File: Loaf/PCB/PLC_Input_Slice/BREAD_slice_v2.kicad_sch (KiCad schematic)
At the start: 26 parts, among them J1 10018783-10200TLF, J3 DB25_Socket, U1 MCP4922-EP, U2 MCP4922-EP, U3 MCP4922-EP, U4 MCP4922-EP, U5 MCP3208, U6 MCP2561-E-P, U7 MCP2515-xSO, Y1 16MHZ Crystal

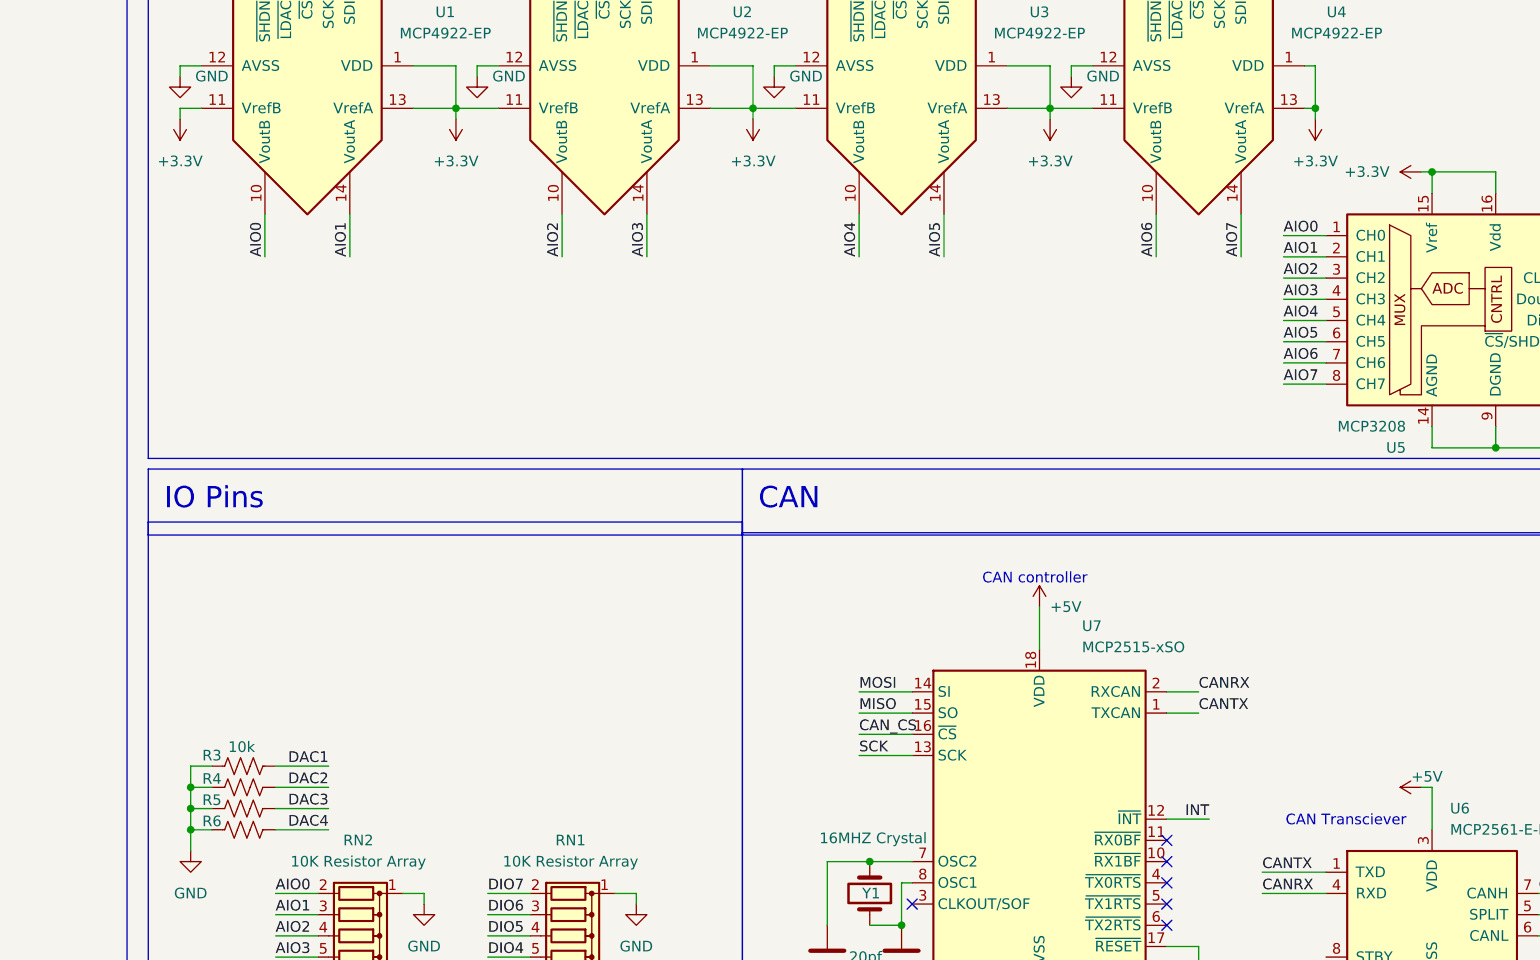
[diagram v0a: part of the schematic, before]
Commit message: Added optional VRM and switched to 5V ADC and DAC
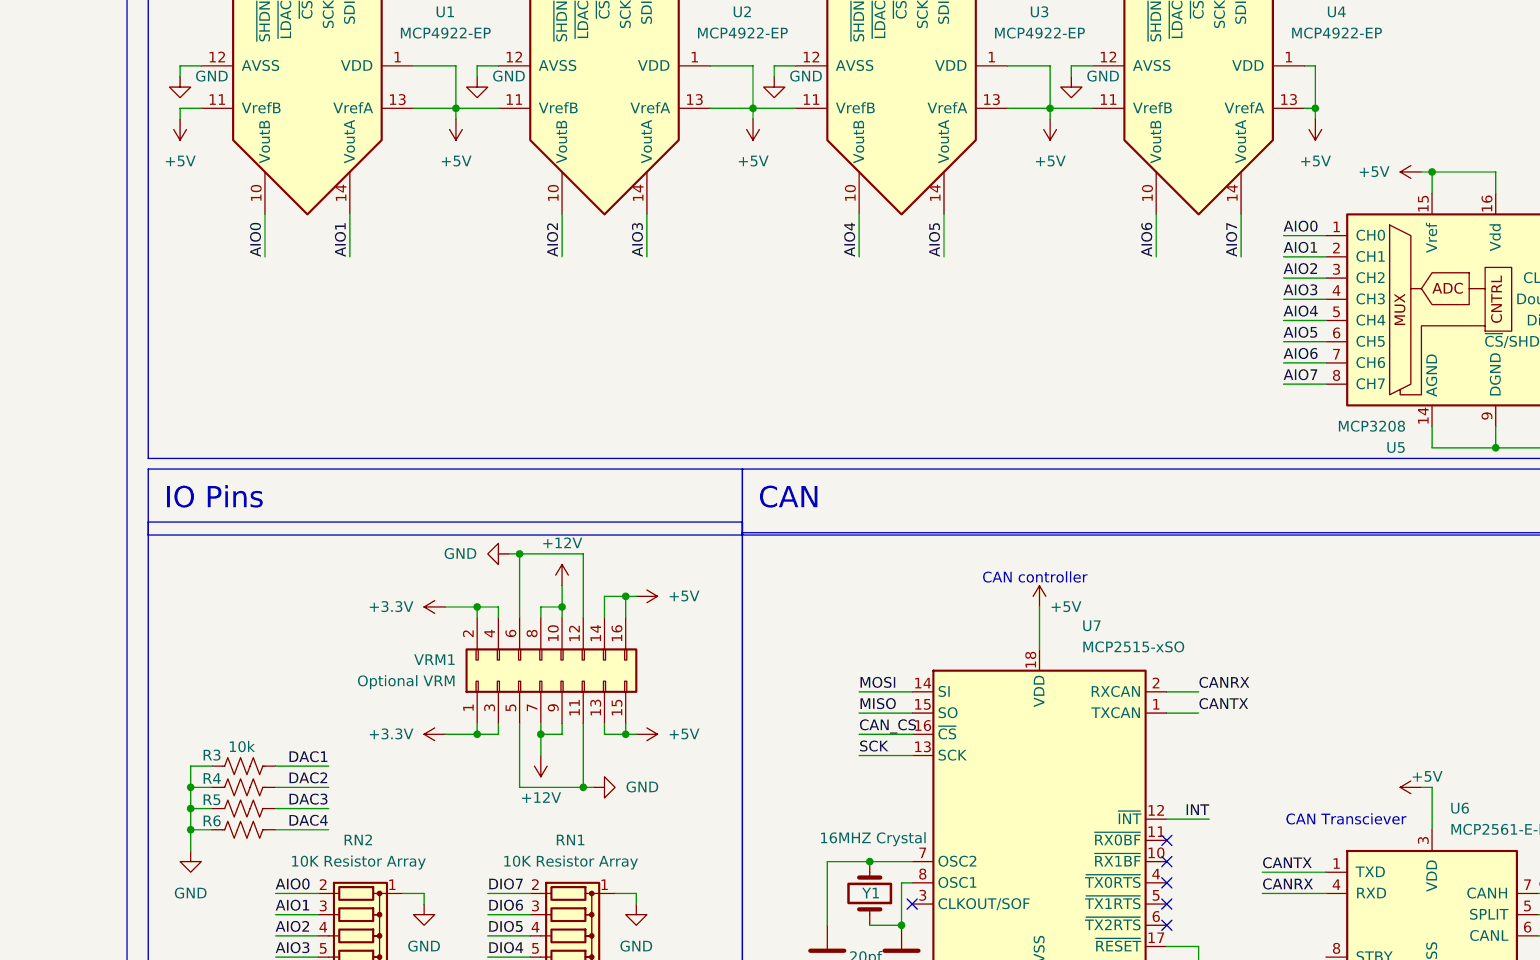
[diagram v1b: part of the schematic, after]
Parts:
- added VRM1: Optional VRM, PinSocket_2x08_P2.54mm_Vertical, symbol Connector_Generic:Conn_02x08_Odd_Even
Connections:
- net +12V: now also VRM1.10 (Pin_10), VRM1.7 (Pin_7), VRM1.8 (Pin_8), VRM1.9 (Pin_9)
- net +3.3V: now also VRM1.1 (Pin_1), VRM1.2 (Pin_2), VRM1.3 (Pin_3), VRM1.4 (Pin_4); no longer U1.1 (VDD), U1.11 (VrefB), U1.13 (VrefA), U2.1 (VDD), U2.11 (VrefB), U2.13 (VrefA), U3.1 (VDD), U3.11 (VrefB), U3.13 (VrefA), U4.1 (VDD), U4.11 (VrefB), U4.13 (VrefA), U5.15 (Vref), U5.16 (Vdd)
- net +5V: now also U1.1 (VDD), U1.11 (VrefB), U1.13 (VrefA), U2.1 (VDD), U2.11 (VrefB), U2.13 (VrefA), U3.1 (VDD), U3.11 (VrefB), U3.13 (VrefA), U4.1 (VDD), U4.11 (VrefB), U4.13 (VrefA), U5.15 (Vref), U5.16 (Vdd), VRM1.13 (Pin_13), VRM1.14 (Pin_14), VRM1.15 (Pin_15), VRM1.16 (Pin_16)
- net GND: now also VRM1.11 (Pin_11), VRM1.12 (Pin_12), VRM1.5 (Pin_5), VRM1.6 (Pin_6)

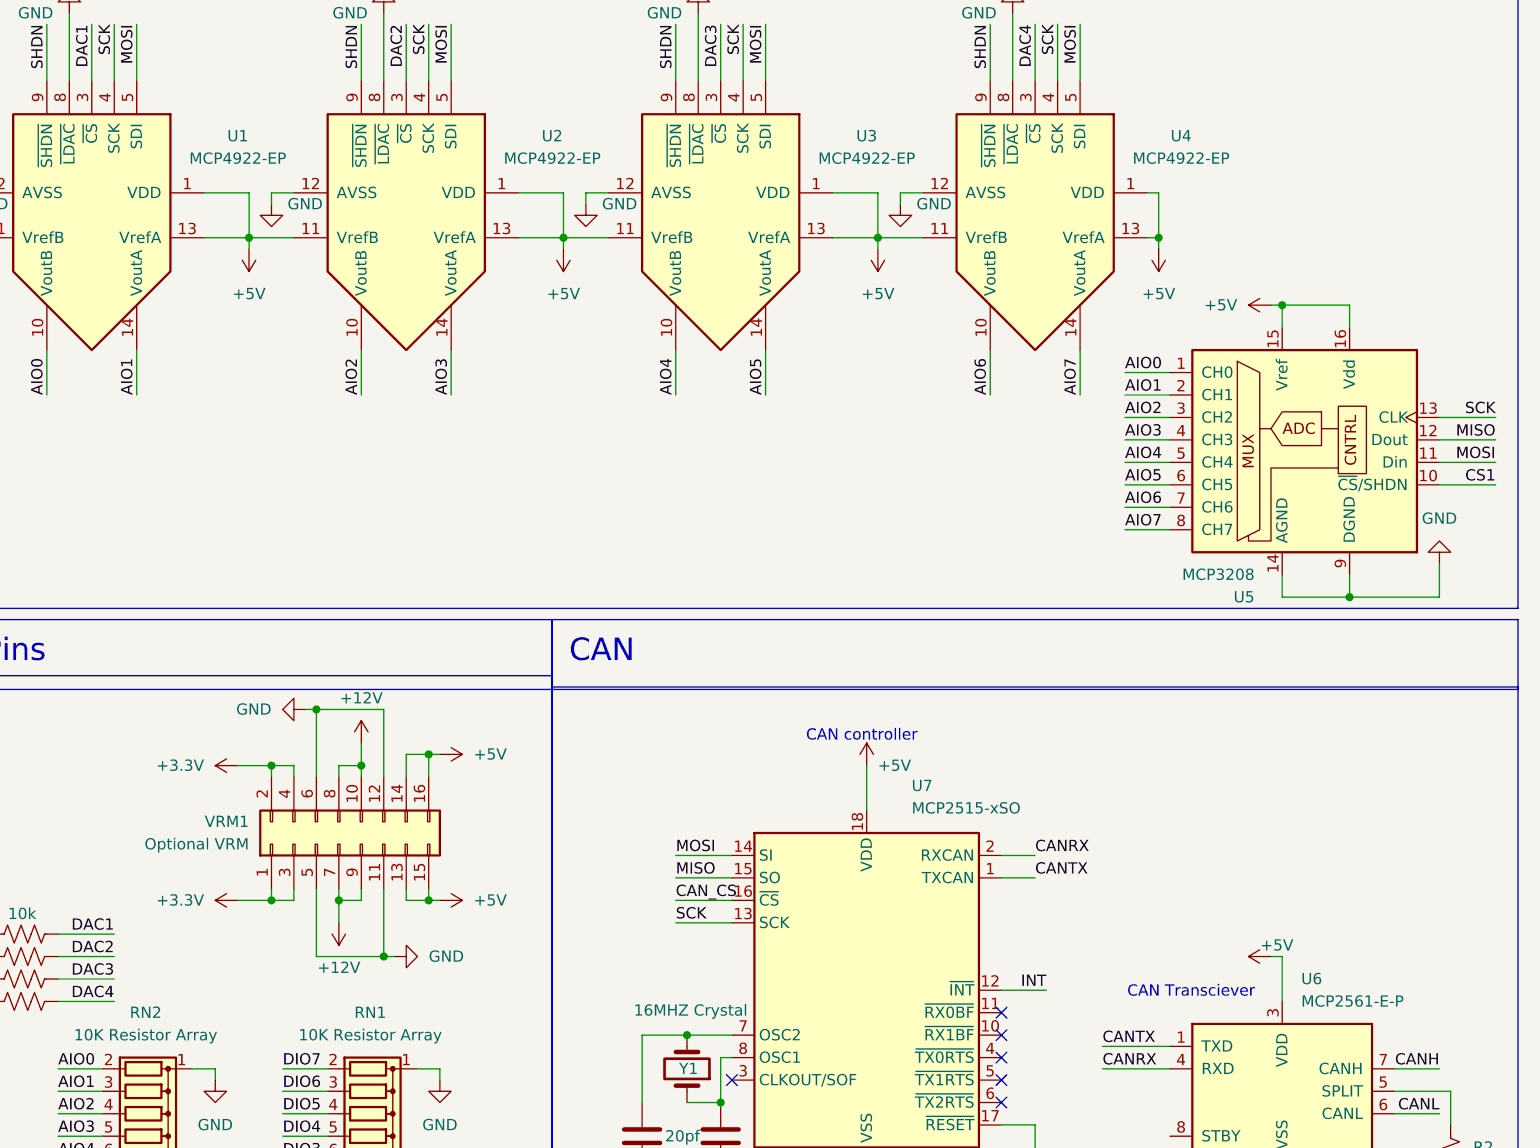
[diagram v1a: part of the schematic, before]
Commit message: Added power filter caps
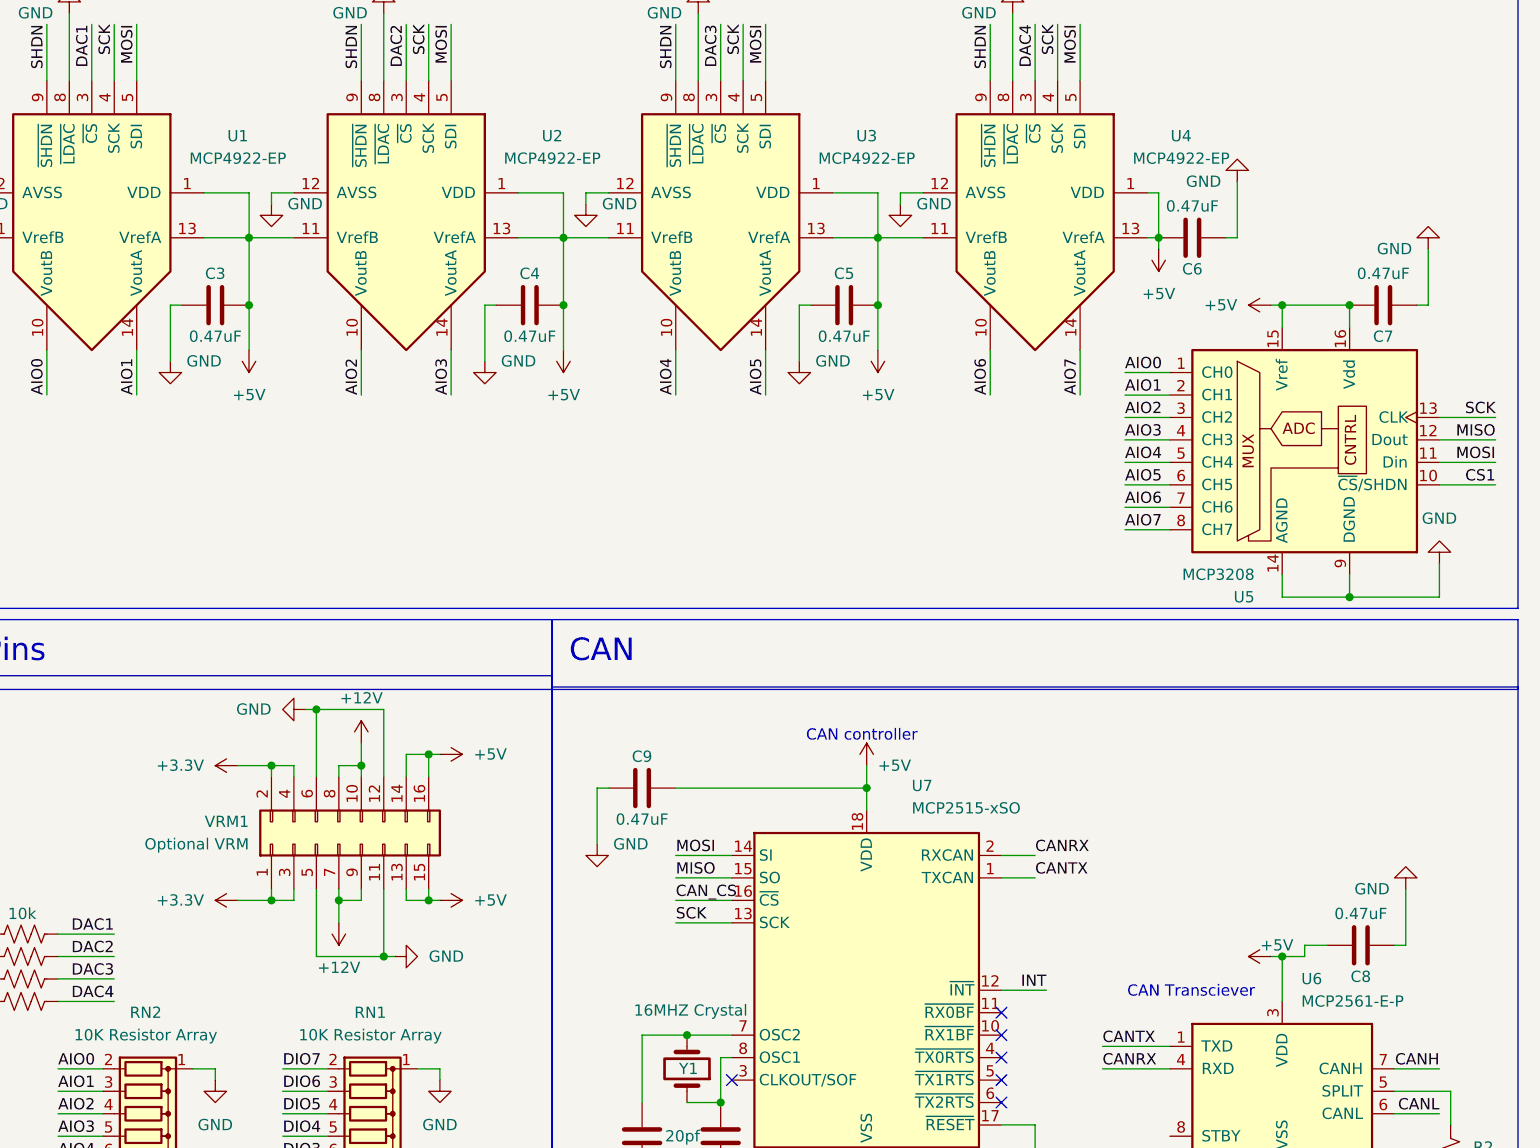
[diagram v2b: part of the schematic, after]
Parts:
- added C3, C4, C5, C6, C7, C8, C9: 0.47uF, C_1206_3216Metric_Pad1.33x1.80mm_HandSolder, symbol Device:C
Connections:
- net +5V: now also C3.2, C4.2, C5.2, C6.2, C7.2, C8.2, C9.2
- net GND: now also C3.1, C4.1, C5.1, C6.1, C7.1, C8.1, C9.1

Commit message: Add files via upload
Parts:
- added J2: Barrel_Jack, Connector_BarrelJack:BarrelJack_SwitchcraftConxall_RAPC10U_Horizontal, symbol Connector:Barrel_Jack
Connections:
- net +12V: now also J2.1
- net +3.3V: now also VRM1.15 (Pin_15), VRM1.16 (Pin_16); no longer VRM1.3 (Pin_3), VRM1.4 (Pin_4)
- net +5V: now also VRM1.3 (Pin_3), VRM1.4 (Pin_4); no longer VRM1.15 (Pin_15), VRM1.16 (Pin_16)
- net GND: now also J2.2
